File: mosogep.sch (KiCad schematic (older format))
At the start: 47 parts, among them J1 Programozó csati, SW1 SW_DIP_x01, SW2 SW_DIP_x01, U1 24AA02-OT, U2 STM32F030C6Tx, Y1 8MHz

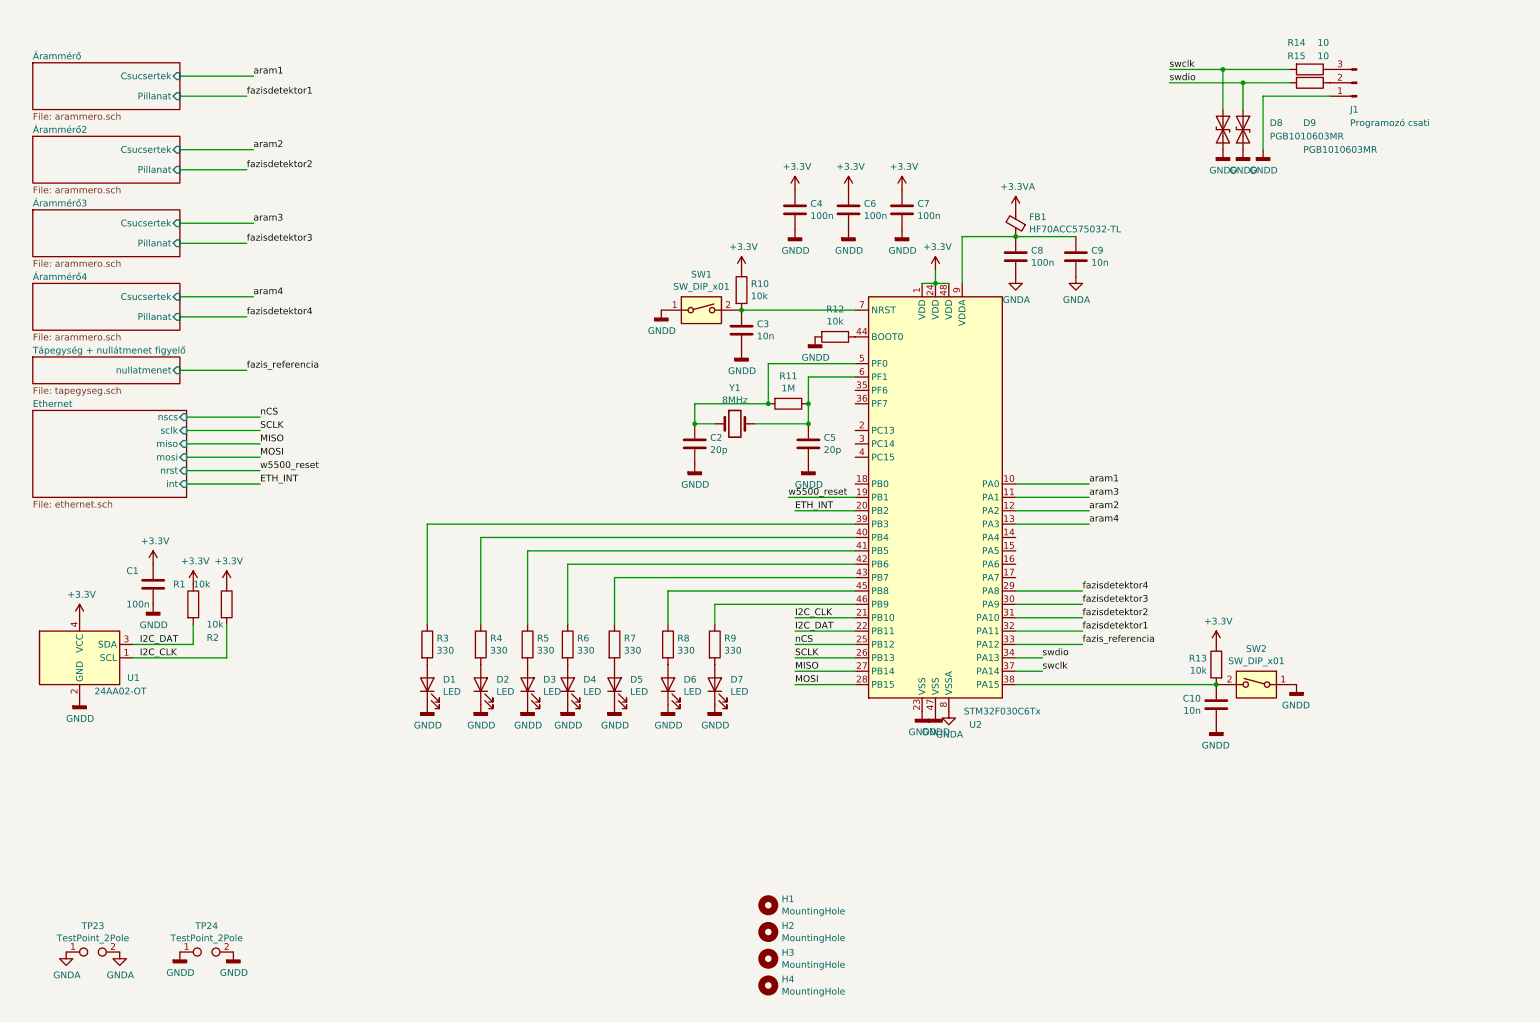
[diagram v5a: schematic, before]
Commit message: Bottom silk
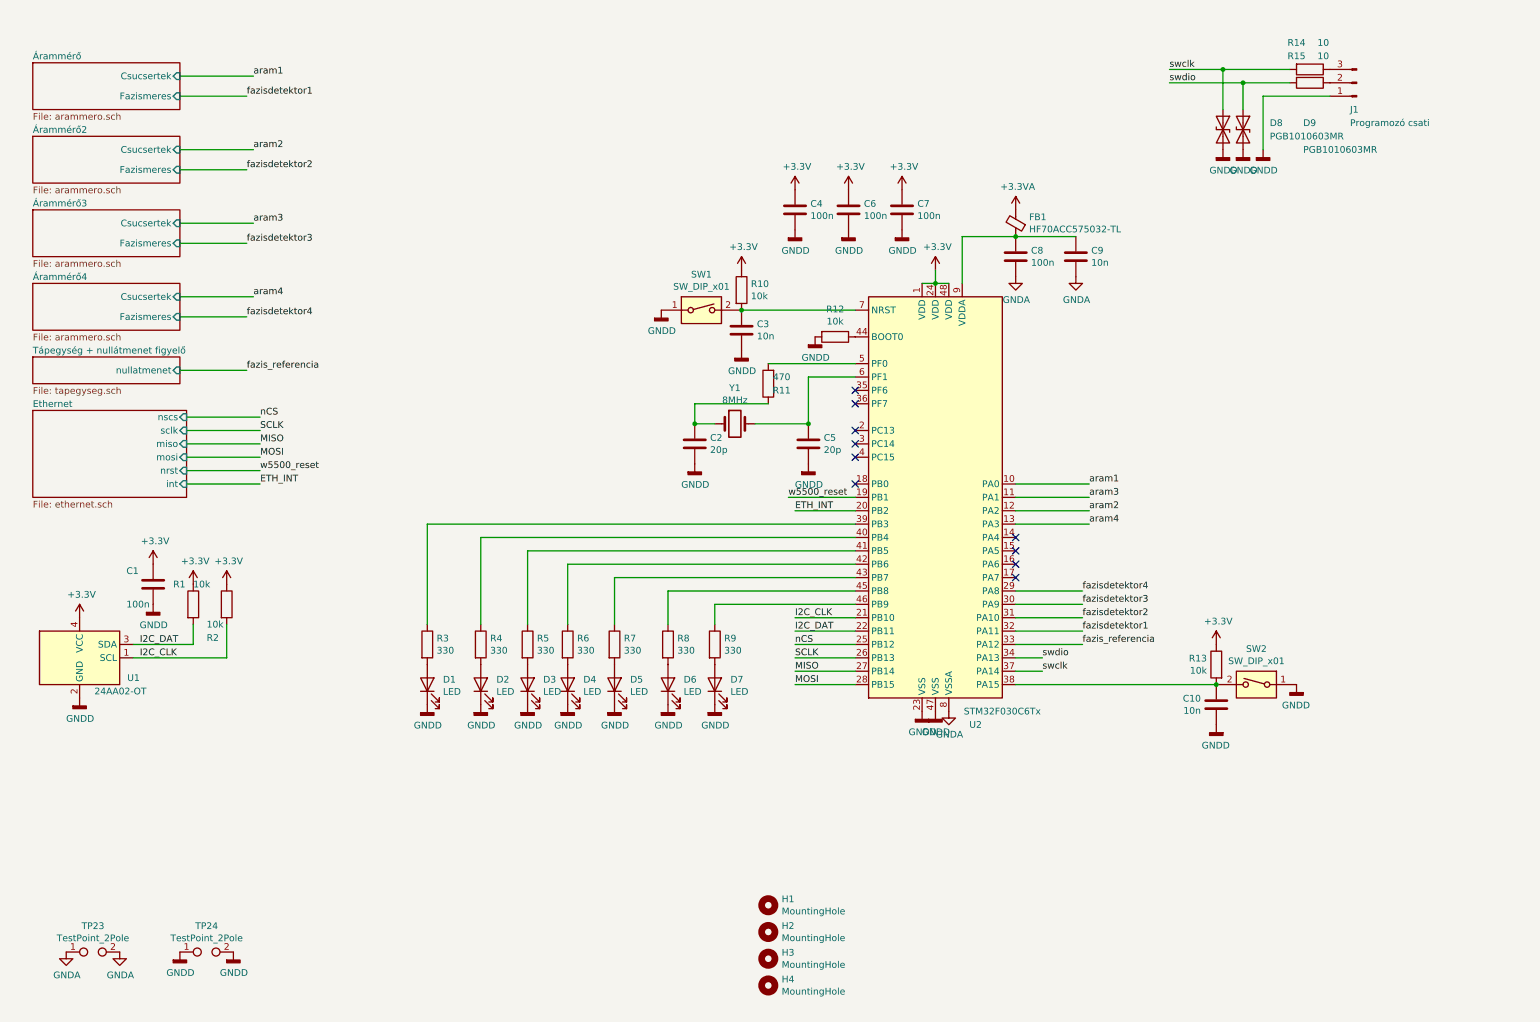
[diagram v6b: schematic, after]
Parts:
- R11: value 1M -> 470
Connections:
- net at R11.2, U2.5 (PF0): no longer C2.1, Y1.1
- net at C5.1, U2.6 (PF1), Y1.2: no longer R11.1
- new net: C2.1, R11.1, Y1.1
- no-connect marks 0 -> 10
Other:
- moved on the sheet: R11
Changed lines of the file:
@@
 	5600 3250 6150 3250
-Wire Wire Line
-	6150 3250 6150 2950
 Wire Wire Line
 	6150 2950 6800 2950
@@
 L Device:R R11
 U 1 1 5E82E9D8
-P 6300 3250
-F 0 "R11" V 6093 3250 50  0000 C CNN
-F 1 "1M" V 6184 3250 50  0000 C CNN
-F 2 "Resistor_SMD:R_0805_2012Metric_Pad1.20x1.40mm_HandSolder" V 6230 3250 50  0001 C CNN
-F 3 "~" H 6300 3250 50  0001 C CNN
-	1    6300 3250
-	0    1    1    0
-$EndComp
-Connection ~ 6150 3250
+P 6150 3100
+F 0 "R11" H 6050 3150 50  0000 C CNN
+F 1 "470" H 6050 3050 50  0000 C CNN
+F 2 "Resistor_SMD:R_0805_2012Metric_Pad1.20x1.40mm_HandSolder" V 6080 3100 50  0001 C CNN
+F 3 "~" H 6150 3100 50  0001 C CNN
+	1    6150 3100
+	-1   0    0    1
+$EndComp
 Wire Wire Line
 	6050 3400 6450 3400
-Wire Wire Line
-	6450 3400 6450 3250
 Connection ~ 6450 3400
 Wire Wire Line
-	6450 3050 6450 3250
-Wire Wire Line
 	6450 3050 6800 3050
-Connection ~ 6450 3250
 $Comp
 L Device:C C4
@@
 	1    0    0    -1
 $EndComp
-$Sheet
-S 650  700  1100 350
-U 5F747DA7
-F0 "Árammérő" 50
-F1 "arammero.sch" 50
-F2 "Csucsertek" I R 1750 800 50
-F3 "Pillanat" I R 1750 950 50
-$EndSheet
 Text Label 9150 850  0    50   ~ 0
 swdio
@@
 Text Label 2350 3850 0    50   ~ 0
 ETH_INT
-$Sheet
-S 650  1250 1100 350
-U 5F79F032
-F0 "Árammérő2" 50
-F1 "arammero.sch" 50
-F2 "Csucsertek" I R 1750 1350 50
-F3 "Pillanat" I R 1750 1500 50
-$EndSheet
-$Sheet
-S 650  1800 1100 350
-U 5F7A6B7B
-F0 "Árammérő3" 50
-F1 "arammero.sch" 50
-F2 "Csucsertek" I R 1750 1900 50
-F3 "Pillanat" I R 1750 2050 50
-$EndSheet
-$Sheet
-S 650  2350 1100 350
-U 5F7B080A
-F0 "Árammérő4" 50
-F1 "arammero.sch" 50
-F2 "Csucsertek" I R 1750 2450 50
-F3 "Pillanat" I R 1750 2600 50
-$EndSheet
 Text Label 6300 3950 0    50   ~ 0
 w5500_reset
@@
 	1    0    0    -1
 $EndComp
+NoConn ~ 8000 4250
+Wire Wire Line
+	6450 3050 6450 3400
+NoConn ~ 8000 4350
+NoConn ~ 8000 4450
+NoConn ~ 8000 4550
+NoConn ~ 6800 3150
+NoConn ~ 6800 3250
+NoConn ~ 6800 3450
+NoConn ~ 6800 3550
+NoConn ~ 6800 3650
+NoConn ~ 6800 3850
+$Sheet
+S 650  2350 1100 350
+U 5F7B080A
+F0 "Árammérő4" 50
+F1 "arammero.sch" 50
+F2 "Csucsertek" I R 1750 2450 50
+F3 "Fazismeres" I R 1750 2600 50
+$EndSheet
+$Sheet
+S 650  1800 1100 350
+U 5F7A6B7B
+F0 "Árammérő3" 50
+F1 "arammero.sch" 50
+F2 "Csucsertek" I R 1750 1900 50
+F3 "Fazismeres" I R 1750 2050 50
+$EndSheet
+$Sheet
+S 650  1250 1100 350
+U 5F79F032
+F0 "Árammérő2" 50
+F1 "arammero.sch" 50
+F2 "Csucsertek" I R 1750 1350 50
+F3 "Fazismeres" I R 1750 1500 50
+$EndSheet
+$Sheet
+S 650  700  1100 350
+U 5F747DA7
+F0 "Árammérő" 50
+F1 "arammero.sch" 50
+F2 "Csucsertek" I R 1750 800 50
+F3 "Fazismeres" I R 1750 950 50
+$EndSheet
 $EndSCHEMATC
